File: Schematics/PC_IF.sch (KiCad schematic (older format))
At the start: 4 parts, among them U22 74F377, U23 74F377

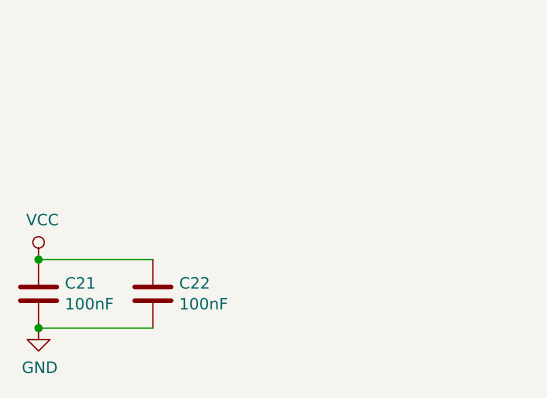
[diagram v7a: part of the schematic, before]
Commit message: Pack parts neatly into a smaller board size.
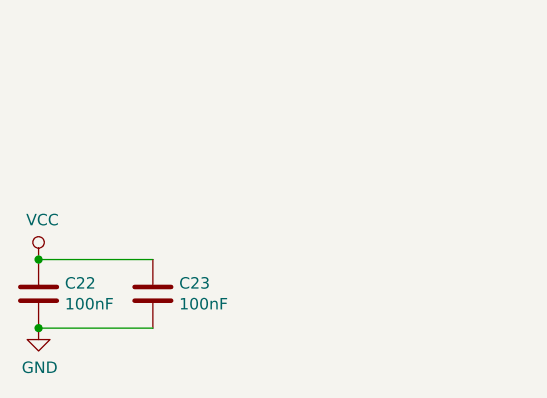
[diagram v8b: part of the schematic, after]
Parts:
- renumbered C21 to C22, C22 to C23
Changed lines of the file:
@@
 $EndComp
 $Comp
-L power:VCC #PWR054
+L power:VCC #PWR056
 U 1 1 5DD10B91
 P 5500 1750
-F 0 "#PWR054" H 5500 1600 50  0001 C CNN
+F 0 "#PWR056" H 5500 1600 50  0001 C CNN
 F 1 "VCC" H 5517 1923 50  0000 C CNN
 F 2 "" H 5500 1750 50  0001 C CNN
@@
 $EndComp
 $Comp
-L power:VCC #PWR056
+L power:VCC #PWR058
 U 1 1 5DD11404
 P 5500 3900
-F 0 "#PWR056" H 5500 3750 50  0001 C CNN
+F 0 "#PWR058" H 5500 3750 50  0001 C CNN
 F 1 "VCC" H 5517 4073 50  0000 C CNN
 F 2 "" H 5500 3900 50  0001 C CNN
@@
 $EndComp
 $Comp
-L power:GND #PWR055
+L power:GND #PWR057
 U 1 1 5DD11B50
 P 5500 3350
-F 0 "#PWR055" H 5500 3100 50  0001 C CNN
+F 0 "#PWR057" H 5500 3100 50  0001 C CNN
 F 1 "GND" H 5505 3177 50  0000 C CNN
 F 2 "" H 5500 3350 50  0001 C CNN
@@
 $EndComp
 $Comp
-L power:GND #PWR057
+L power:GND #PWR059
 U 1 1 5DD12126
 P 5500 5500
-F 0 "#PWR057" H 5500 5250 50  0001 C CNN
+F 0 "#PWR059" H 5500 5250 50  0001 C CNN
 F 1 "GND" H 5505 5327 50  0000 C CNN
 F 2 "" H 5500 5500 50  0001 C CNN
@@
 	5000 5100 3400 5100
 $Comp
-L power:GND #PWR053
+L power:GND #PWR055
 U 1 1 5DD12CA4
 P 5000 5200
-F 0 "#PWR053" H 5000 4950 50  0001 C CNN
+F 0 "#PWR055" H 5000 4950 50  0001 C CNN
 F 1 "GND" V 5005 5072 50  0000 R CNN
 F 2 "" H 5000 5200 50  0001 C CNN
@@
 $EndComp
 $Comp
-L power:GND #PWR052
+L power:GND #PWR054
 U 1 1 5DD131DF
 P 5000 3050
-F 0 "#PWR052" H 5000 2800 50  0001 C CNN
+F 0 "#PWR054" H 5000 2800 50  0001 C CNN
 F 1 "GND" V 5005 2922 50  0000 R CNN
 F 2 "" H 5000 3050 50  0001 C CNN
@@
 	8850 5500 6600 5500
 $Comp
-L Device:C C21
+L Device:C C22
 U 1 1 5DD31495
 P 1000 7150
-F 0 "C21" H 1115 7196 50  0000 L CNN
+F 0 "C22" H 1115 7196 50  0000 L CNN
 F 1 "100nF" H 1115 7105 50  0000 L CNN
 F 2 "Capacitor_THT:C_Disc_D4.3mm_W1.9mm_P5.00mm" H 1038 7000 50  0001 C CNN
@@
 $EndComp
 $Comp
-L Device:C C22
+L Device:C C23
 U 1 1 5DD3149B
 P 1500 7150
-F 0 "C22" H 1615 7196 50  0000 L CNN
+F 0 "C23" H 1615 7196 50  0000 L CNN
 F 1 "100nF" H 1615 7105 50  0000 L CNN
 F 2 "Capacitor_THT:C_Disc_D4.3mm_W1.9mm_P5.00mm" H 1538 7000 50  0001 C CNN
@@
 $EndComp
 $Comp
-L power:GND #PWR051
+L power:GND #PWR053
 U 1 1 5DD314A1
 P 1000 7300
-F 0 "#PWR051" H 1000 7050 50  0001 C CNN
+F 0 "#PWR053" H 1000 7050 50  0001 C CNN
 F 1 "GND" H 1005 7127 50  0000 C CNN
 F 2 "" H 1000 7300 50  0001 C CNN
@@
 $EndComp
 $Comp
-L power:VCC #PWR050
+L power:VCC #PWR052
 U 1 1 5DD314A7
 P 1000 7000
-F 0 "#PWR050" H 1000 6850 50  0001 C CNN
+F 0 "#PWR052" H 1000 6850 50  0001 C CNN
 F 1 "VCC" H 1017 7173 50  0000 C CNN
 F 2 "" H 1000 7000 50  0001 C CNN
